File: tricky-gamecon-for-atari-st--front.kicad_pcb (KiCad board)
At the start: 2 copper layers, 109.2 x 45.7 mm, 10 parts

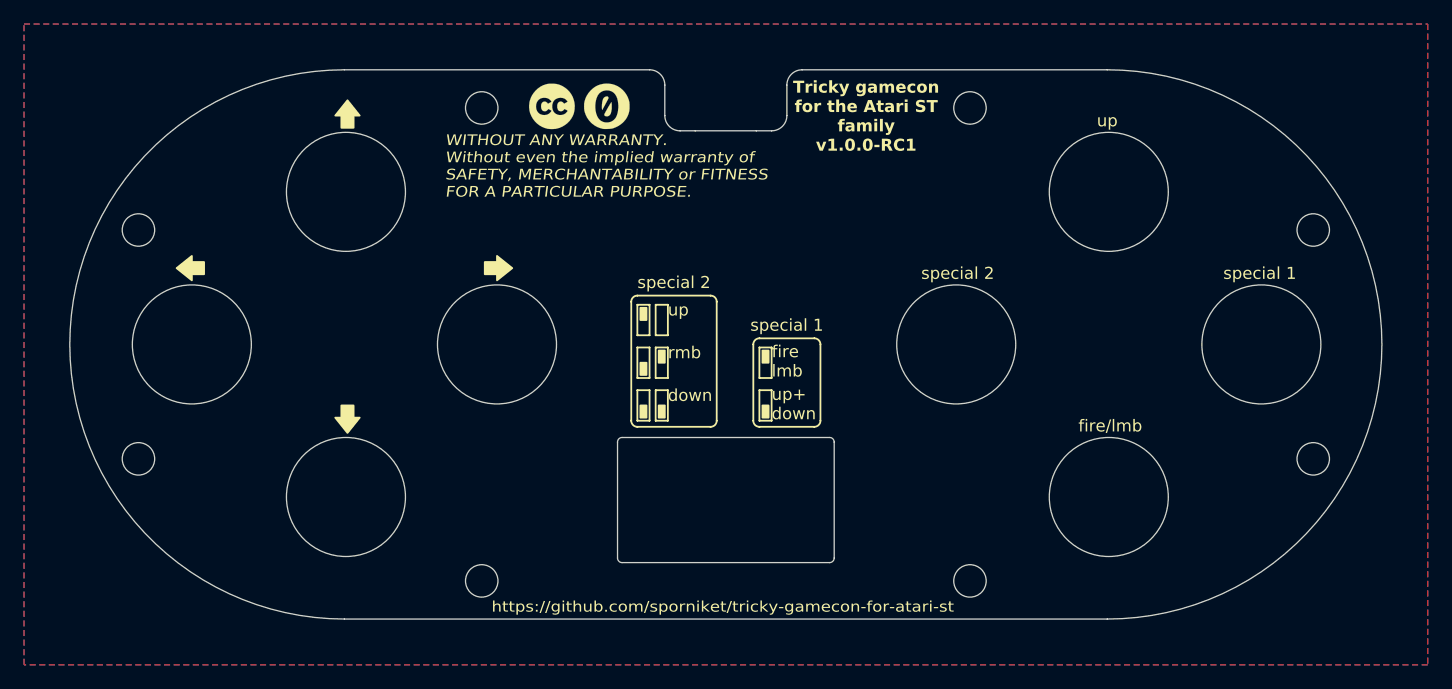
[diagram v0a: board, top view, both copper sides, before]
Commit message: fixes push button holes, text size and position
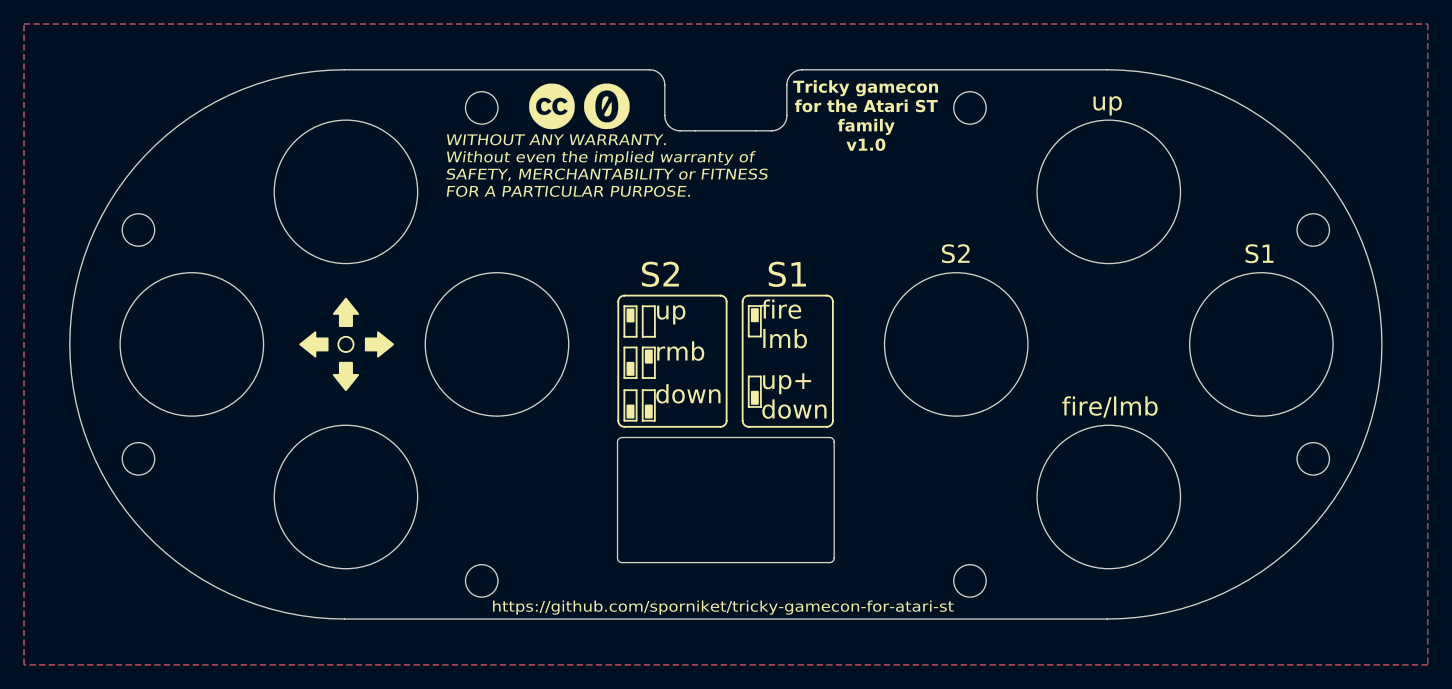
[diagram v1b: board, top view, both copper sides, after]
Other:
- outline, holes or cut-outs redrawn
- board text added: "S1"
- board text added: "S2"
- board text added: "Tricky gamecon for the Atari ST family v1.0"
- board text removed: "Tricky gamecon for the Atari ST family v1.0.0-RC1"
- board text removed: "special 1"
- board text removed: "special 2"
